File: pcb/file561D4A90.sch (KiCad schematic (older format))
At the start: 22 parts

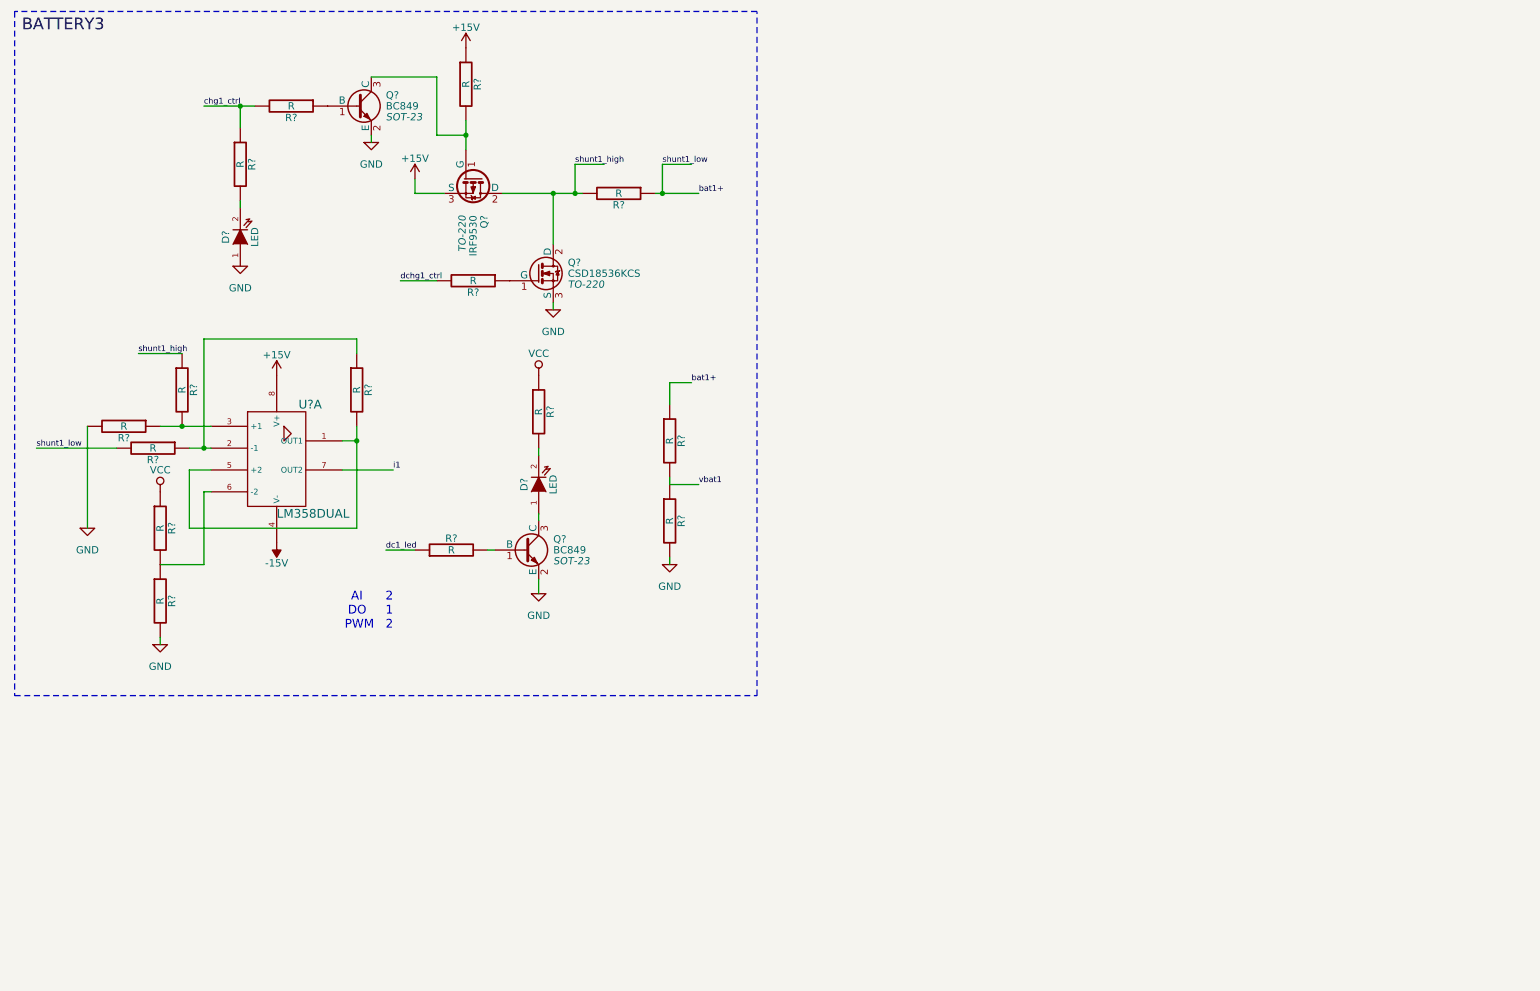
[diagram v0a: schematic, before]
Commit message: updated schematics
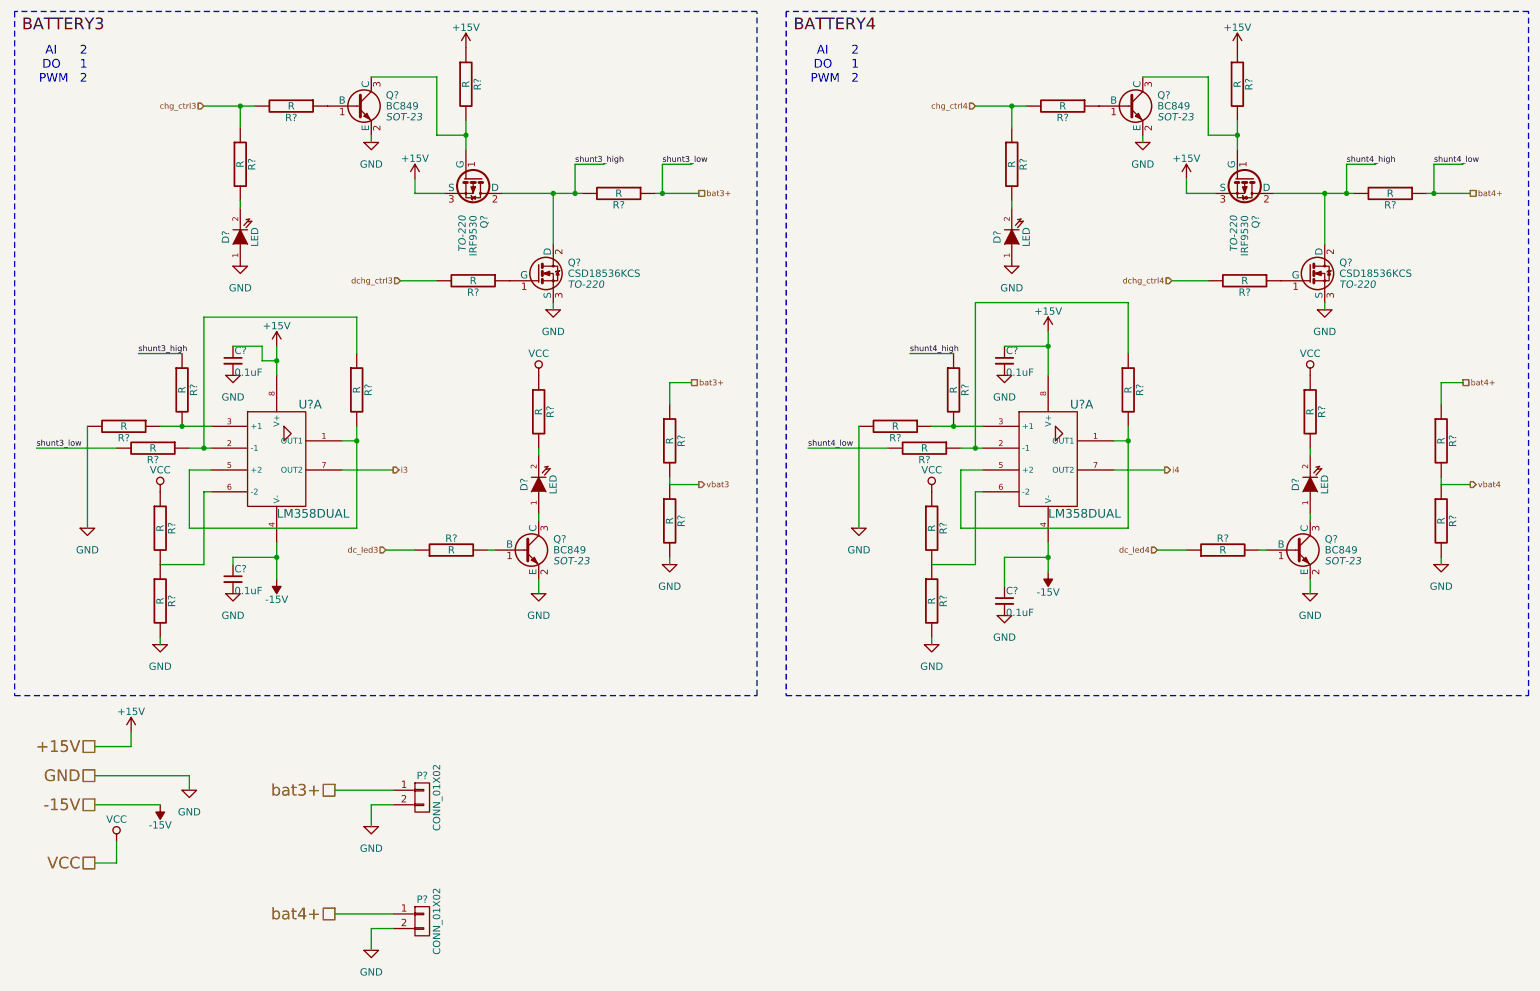
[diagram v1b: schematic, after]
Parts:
- added C? (x4): 0.1uF, symbol C_Small
- added D? (x2): LED, symbol LED-RESCUE-BatAger
- added P? (x2): CONN_01X02, symbol CONN_01X02
- added Q? (x2): BC849, SOT-23, symbol BC849
- added Q?: CSD18536KCS, TO-220, symbol BTS141
- added Q?: IRF9530, TO-220, symbol IRF9530
- added R? (x15): R, symbol R-RESCUE-BatAger
- added U?: LM358DUAL, symbol LM358Dual
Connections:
- net labels added: BATTERY4, bat3+, bat4+, chg_ctrl3, chg_ctrl4, dc_led3, dc_led4, dchg_ctrl3, dchg_ctrl4, i3, i4, shunt3_high, shunt3_low, shunt4_high, shunt4_low, vbat3, vbat4
- net labels removed: bat1+, chg1_ctrl, dc1_led, dchg1_ctrl, i1, shunt1_high, shunt1_low, vbat1
- wire segments 47 -> 119

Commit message: starting on layout
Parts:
- C17, C18, C19, C20: renamed from C?; footprint (none) -> Capacitors_SMD:C_0805_HandSoldering
- D5, D6, D7, D8: renamed from D?; footprint (none) -> LEDs:LED-0805
- P10, P11: renamed from P?; footprint (none) -> Pin_Headers:Pin_Header_Straight_1x02
- Q10, Q12, Q14, Q16: renamed from Q?; footprint SOT-23 -> Housings_SOT-23_SOT-143_TSOT-6:SOT-23_Handsoldering
- Q11, Q13, Q15, Q17: renamed from Q?; footprint TO-220 -> Power_Integrations:TO-220
- R37, R38, R39, R40, R41, R44, R50, R51, R52, R53, R54, R55, R56, R59, R65, R66: renamed from R?; footprint (none) -> Resistors_ThroughHole:Resistor_Horizontal_RM10mm
- R42, R43, R45, R46, R47, R48, R57, R58, R60, R62, R63: renamed from R?; footprint (none) -> Resistors_SMD:R_0805_HandSoldering
- R49, R64: renamed from R?; value R -> 0R056; footprint (none) -> Resistors_SMD:R_2512_HandSoldering; Part # (none) -> RL2512 FK-07 0R056
- R61: renamed from R?; footprint (none) -> Resistors_SMD:R_2512_HandSoldering
- U4, U5: renamed from U?; footprint (none) -> Housings_SOIC:SOIC-8_3.9x4.9mm_Pitch1.27mm
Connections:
- net at R53.1, R59.1: now also U5.6 (-2); no longer U5.2 (-1)
- net at R52.1, R56.2: now also U5.5 (+2); no longer U5.3 (+1)
- new net: R59.2, U5.5 (+2), U5.7 (OUT2)

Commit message: trace complete (maybe!)
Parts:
- R61: footprint Resistors_SMD:R_2512_HandSoldering -> Resistors_SMD:R_0805_HandSoldering
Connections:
- net at R59.2, U5.5 (+2): now also U5.1 (OUT1); no longer U5.7 (OUT2)
- net at R52.1, R56.2: now also U5.3 (+1); no longer U5.5 (+2)
- net at R53.1, R59.1: now also U5.2 (-1); no longer U5.6 (-2)
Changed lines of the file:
@@
 F 0 "R61" V 9080 1050 50  0000 C CNN
 F 1 "R" V 9000 1050 50  0000 C CNN
-F 2 "Resistors_SMD:R_2512_HandSoldering" V 8930 1050 30  0001 C CNN
+F 2 "Resistors_SMD:R_0805_HandSoldering" V 8930 1050 30  0001 C CNN
 F 3 "" H 9000 1050 30  0000 C CNN
 	1    9000 1050
@@
 $Comp
 L LM358Dual U5
-U 2 1 561D84C9
+U 1 1 561D84C9
 P 7700 3500
 F 0 "U5" H 7850 3750 60  0000 L CNN
@@
 F 2 "Housings_SOIC:SOIC-8_3.9x4.9mm_Pitch1.27mm" H 7700 3500 60  0001 C CNN
 F 3 "" H 7700 3500 60  0000 C CNN
-	2    7700 3500
+	1    7700 3500
 	1    0    0    -1
 $EndComp

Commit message: Production candidate - passes DRC.
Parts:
- R37, R38, R39, R40, R41, R50, R51, R52, R53, R54, R55, R56, R59, R65, R66: footprint Resistors_ThroughHole:Resistor_Horizontal_RM10mm -> Custom Footprints:Resistor_Horizontal_RM10mm
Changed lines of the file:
@@
 F 0 "R51" V 5180 4050 50  0000 C CNN
 F 1 "R" V 5100 4050 50  0000 C CNN
-F 2 "Resistors_ThroughHole:Resistor_Horizontal_RM10mm" V 5030 4050 30  0001 C CNN
+F 2 "Custom Footprints:Resistor_Horizontal_RM10mm" V 5030 4050 30  0001 C CNN
 F 3 "" H 5100 4050 30  0000 C CNN
 	1    5100 4050
@@
 F 0 "R50" V 5180 3500 50  0000 C CNN
 F 1 "R" V 5100 3500 50  0000 C CNN
-F 2 "Resistors_ThroughHole:Resistor_Horizontal_RM10mm" V 5030 3500 30  0001 C CNN
+F 2 "Custom Footprints:Resistor_Horizontal_RM10mm" V 5030 3500 30  0001 C CNN
 F 3 "" H 5100 3500 30  0000 C CNN
 	1    5100 3500
@@
 F 0 "R41" V 1830 3150 50  0000 C CNN
 F 1 "R" V 1750 3150 50  0000 C CNN
-F 2 "Resistors_ThroughHole:Resistor_Horizontal_RM10mm" V 1680 3150 30  0001 C CNN
+F 2 "Custom Footprints:Resistor_Horizontal_RM10mm" V 1680 3150 30  0001 C CNN
 F 3 "" H 1750 3150 30  0000 C CNN
 	1    1750 3150
@@
 F 0 "R37" V 1430 3400 50  0000 C CNN
 F 1 "R" V 1350 3400 50  0000 C CNN
-F 2 "Resistors_ThroughHole:Resistor_Horizontal_RM10mm" V 1280 3400 30  0001 C CNN
+F 2 "Custom Footprints:Resistor_Horizontal_RM10mm" V 1280 3400 30  0001 C CNN
 F 3 "" H 1350 3400 30  0000 C CNN
 	1    1350 3400
@@
 F 0 "R38" V 1630 3550 50  0000 C CNN
 F 1 "R" V 1550 3550 50  0000 C CNN
-F 2 "Resistors_ThroughHole:Resistor_Horizontal_RM10mm" V 1480 3550 30  0001 C CNN
+F 2 "Custom Footprints:Resistor_Horizontal_RM10mm" V 1480 3550 30  0001 C CNN
 F 3 "" H 1550 3550 30  0000 C CNN
 	1    1550 3550
@@
 F 0 "R39" V 1680 4100 50  0000 C CNN
 F 1 "R" V 1600 4100 50  0000 C CNN
-F 2 "Resistors_ThroughHole:Resistor_Horizontal_RM10mm" V 1530 4100 30  0001 C CNN
+F 2 "Custom Footprints:Resistor_Horizontal_RM10mm" V 1530 4100 30  0001 C CNN
 F 3 "" H 1600 4100 30  0000 C CNN
 	1    1600 4100
@@
 F 0 "R40" V 1680 4600 50  0000 C CNN
 F 1 "R" V 1600 4600 50  0000 C CNN
-F 2 "Resistors_ThroughHole:Resistor_Horizontal_RM10mm" V 1530 4600 30  0001 C CNN
+F 2 "Custom Footprints:Resistor_Horizontal_RM10mm" V 1530 4600 30  0001 C CNN
 F 3 "" H 1600 4600 30  0000 C CNN
 	1    1600 4600
@@
 F 0 "R66" V 10480 4050 50  0000 C CNN
 F 1 "R" V 10400 4050 50  0000 C CNN
-F 2 "Resistors_ThroughHole:Resistor_Horizontal_RM10mm" V 10330 4050 30  0001 C CNN
+F 2 "Custom Footprints:Resistor_Horizontal_RM10mm" V 10330 4050 30  0001 C CNN
 F 3 "" H 10400 4050 30  0000 C CNN
 	1    10400 4050
@@
 F 0 "R65" V 10480 3500 50  0000 C CNN
 F 1 "R" V 10400 3500 50  0000 C CNN
-F 2 "Resistors_ThroughHole:Resistor_Horizontal_RM10mm" V 10330 3500 30  0001 C CNN
+F 2 "Custom Footprints:Resistor_Horizontal_RM10mm" V 10330 3500 30  0001 C CNN
 F 3 "" H 10400 3500 30  0000 C CNN
 	1    10400 3500
@@
 F 0 "R56" V 7130 3150 50  0000 C CNN
 F 1 "R" V 7050 3150 50  0000 C CNN
-F 2 "Resistors_ThroughHole:Resistor_Horizontal_RM10mm" V 6980 3150 30  0001 C CNN
+F 2 "Custom Footprints:Resistor_Horizontal_RM10mm" V 6980 3150 30  0001 C CNN
 F 3 "" H 7050 3150 30  0000 C CNN
 	1    7050 3150
@@
 F 0 "R52" V 6730 3400 50  0000 C CNN
 F 1 "R" V 6650 3400 50  0000 C CNN
-F 2 "Resistors_ThroughHole:Resistor_Horizontal_RM10mm" V 6580 3400 30  0001 C CNN
+F 2 "Custom Footprints:Resistor_Horizontal_RM10mm" V 6580 3400 30  0001 C CNN
 F 3 "" H 6650 3400 30  0000 C CNN
 	1    6650 3400
@@
 F 0 "R53" V 6930 3550 50  0000 C CNN
 F 1 "R" V 6850 3550 50  0000 C CNN
-F 2 "Resistors_ThroughHole:Resistor_Horizontal_RM10mm" V 6780 3550 30  0001 C CNN
+F 2 "Custom Footprints:Resistor_Horizontal_RM10mm" V 6780 3550 30  0001 C CNN
 F 3 "" H 6850 3550 30  0000 C CNN
 	1    6850 3550
@@
 F 0 "R59" V 8330 3150 50  0000 C CNN
 F 1 "R" V 8250 3150 50  0000 C CNN
-F 2 "Resistors_ThroughHole:Resistor_Horizontal_RM10mm" V 8180 3150 30  0001 C CNN
+F 2 "Custom Footprints:Resistor_Horizontal_RM10mm" V 8180 3150 30  0001 C CNN
 F 3 "" H 8250 3150 30  0000 C CNN
 	1    8250 3150
@@
 F 0 "R54" V 6980 4100 50  0000 C CNN
 F 1 "R" V 6900 4100 50  0000 C CNN
-F 2 "Resistors_ThroughHole:Resistor_Horizontal_RM10mm" V 6830 4100 30  0001 C CNN
+F 2 "Custom Footprints:Resistor_Horizontal_RM10mm" V 6830 4100 30  0001 C CNN
 F 3 "" H 6900 4100 30  0000 C CNN
 	1    6900 4100
@@
 F 0 "R55" V 6980 4600 50  0000 C CNN
 F 1 "R" V 6900 4600 50  0000 C CNN
-F 2 "Resistors_ThroughHole:Resistor_Horizontal_RM10mm" V 6830 4600 30  0001 C CNN
+F 2 "Custom Footprints:Resistor_Horizontal_RM10mm" V 6830 4600 30  0001 C CNN
 F 3 "" H 6900 4600 30  0000 C CNN
 	1    6900 4600
